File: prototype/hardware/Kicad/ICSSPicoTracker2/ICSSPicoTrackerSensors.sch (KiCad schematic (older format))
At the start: 4 parts, among them U10 SHT1x, U7 MPU-9150, U8 MS5607-02BA, U9 APDS-9306

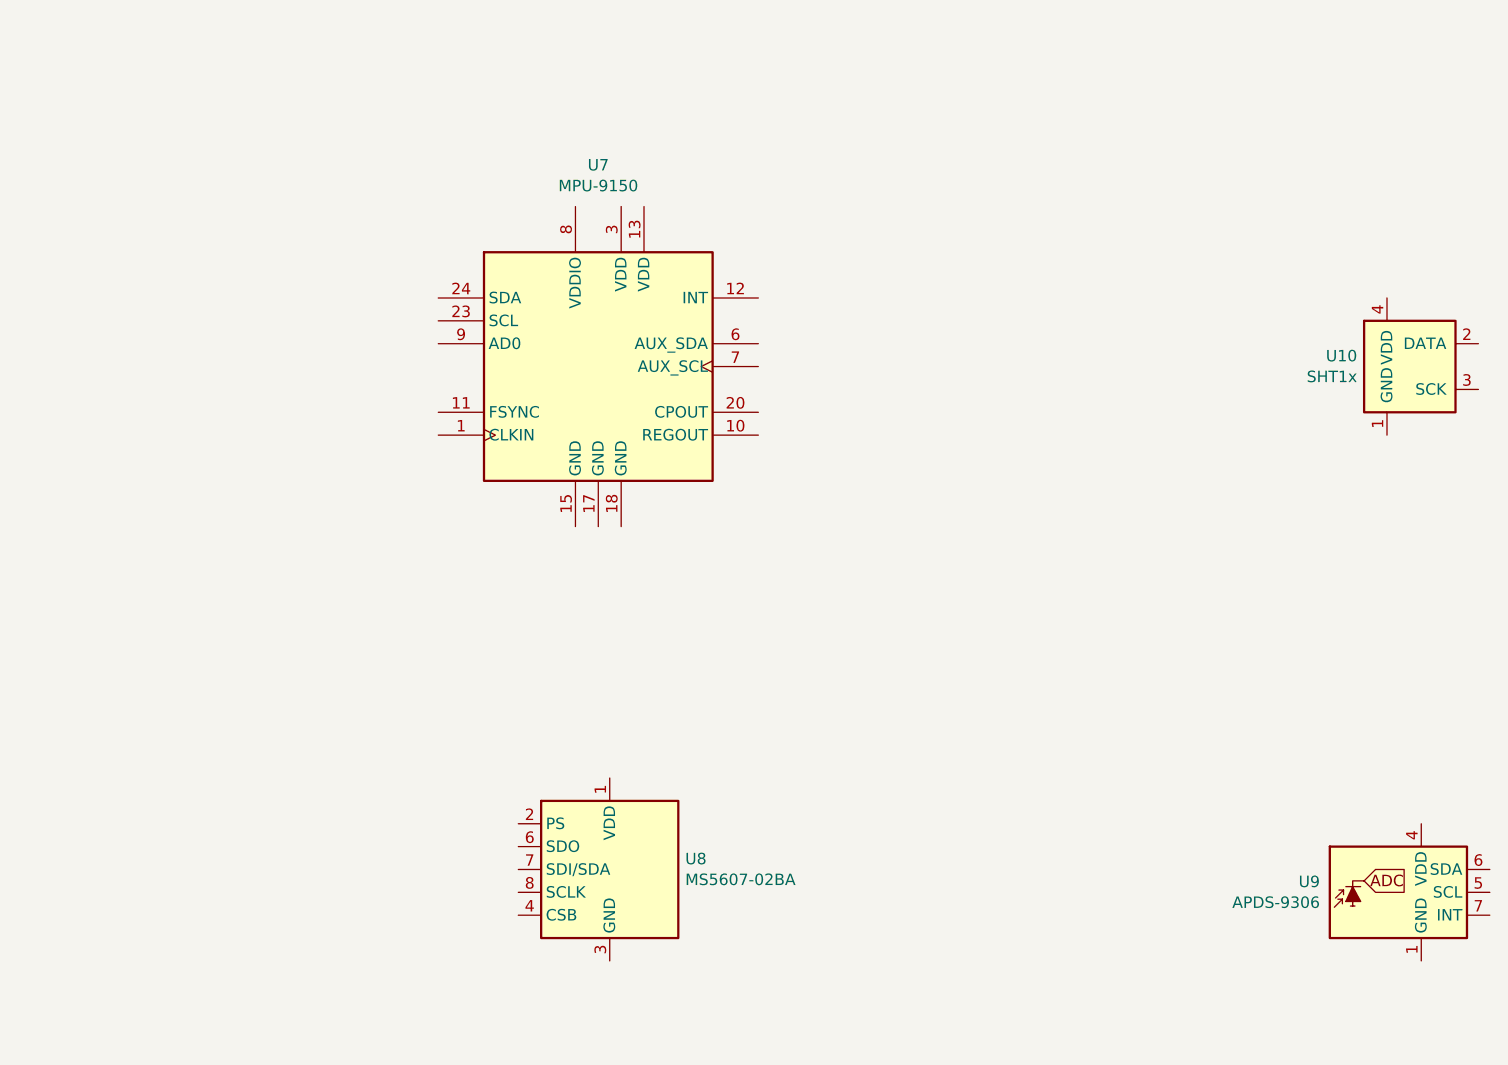
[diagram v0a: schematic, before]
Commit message: Updated Scehematics and Footprints
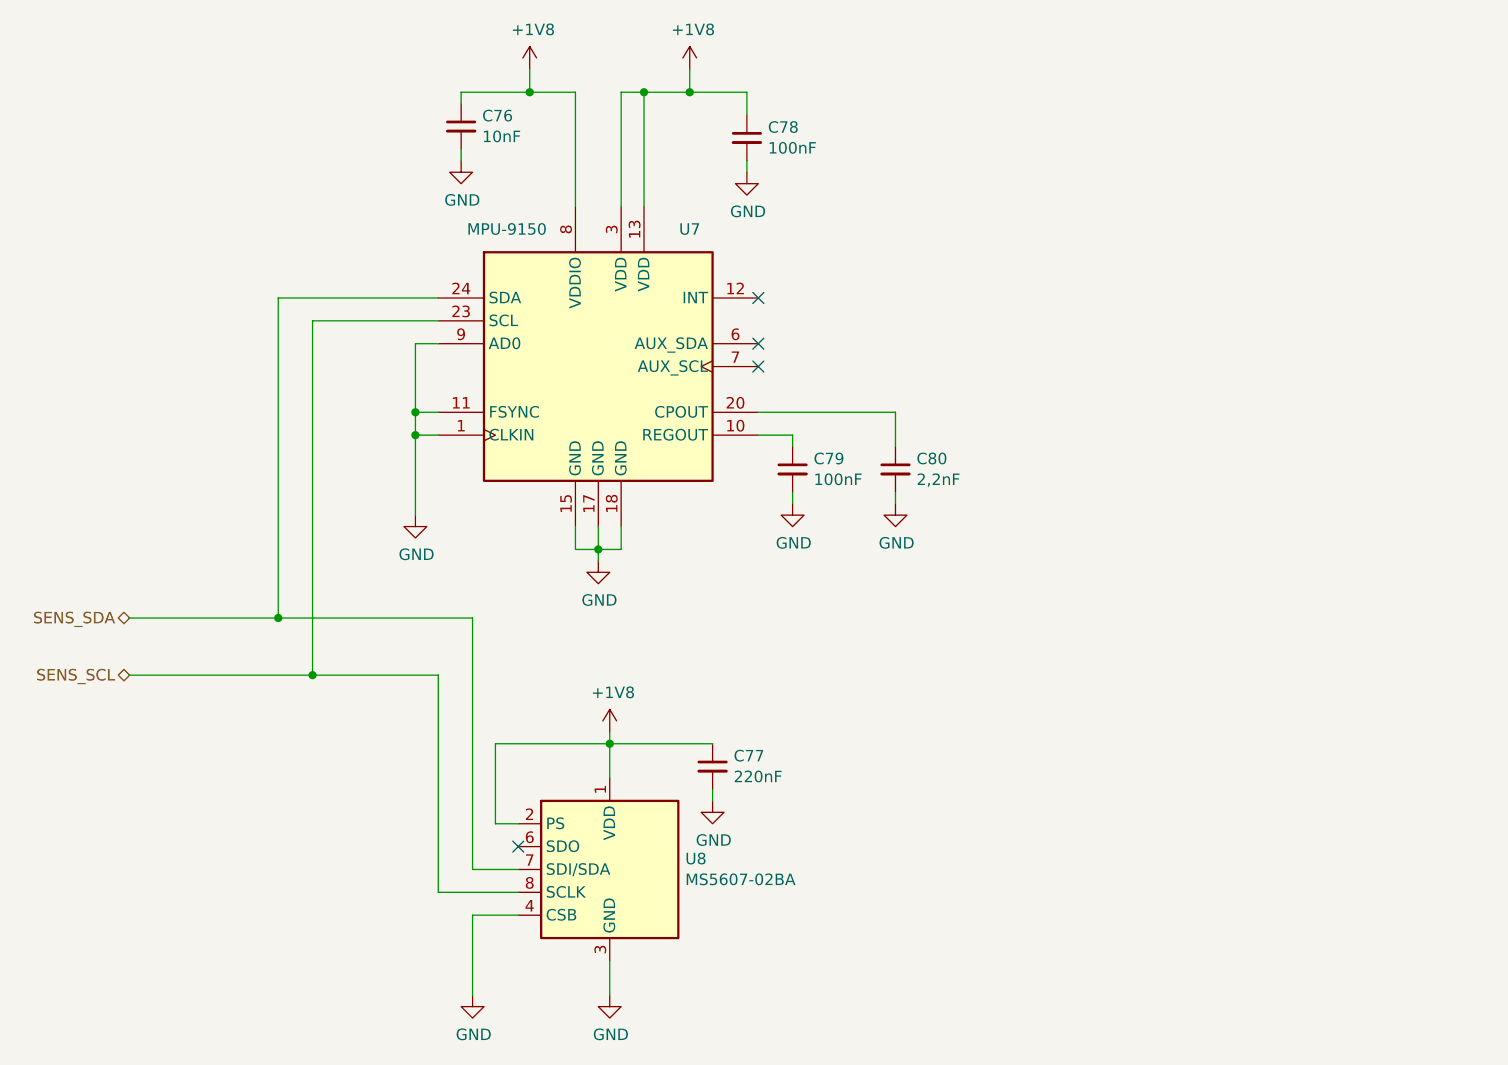
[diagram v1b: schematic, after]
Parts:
- removed U10: SHT1x, Sensor:SHT1x, symbol Sensor:SHT1x
- removed U9: APDS-9306, OptoDevice:Broadcom_LGA-8_2x2mm_P0.53mm, symbol Sensor_Optical:APDS-9306
- added C76: 10nF, Capacitor_SMD:C_0402_1005Metric, symbol Device:C_Small
- added C77: 220nF, Capacitor_SMD:C_0402_1005Metric, symbol Device:C_Small
- added C78, C79: 100nF, Capacitor_SMD:C_0603_1608Metric, symbol Device:C_Small
- added C80: 2,2nF, Capacitor_SMD:C_0402_1005Metric, symbol Device:C_Small
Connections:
- net GND: now reaches U7.1 (CLKIN)
- net GND: now also U7.11 (FSYNC), U7.15 (GND), U7.17 (GND), U7.18 (GND), U7.9 (AD0), U8.3 (GND), U8.4 (CSB), U8.5 (CSB), C76.2, C77.2, C78.2, C79.2, C80.2
- net at U7.10 (REGOUT): now also C79.1
- net +1V8: now reaches U7.13 (VDD)
- net +1V8: now also U7.3 (VDD), U7.8 (VDDIO), U8.1 (VDD), U8.2 (PS), C76.1, C77.1, C78.1
- net at U7.20 (CPOUT): now also C80.1
- net SENS_SCL: now reaches U7.23 (SCL)
- net SENS_SCL: now also U8.8 (SCLK)
- net SENS_SDA: now reaches U7.24 (SDA)
- net SENS_SDA: now also U8.7 (SDI/SDA)
- no-connect marks 0 -> 4
